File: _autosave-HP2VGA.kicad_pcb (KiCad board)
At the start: 4 copper layers, 40.6 x 63 mm, 141 parts, among them CON101 AVR-ISP-6, IC401 ATTINY87-AX, P101 CONN_02X10, P102 CONN_01X07, P103 CONN_02X08, P104 CONN_01X12, P105 CONN_01X02, P106 CONN_01X01, P107 CONN_01X01, P108 CONN_01X01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

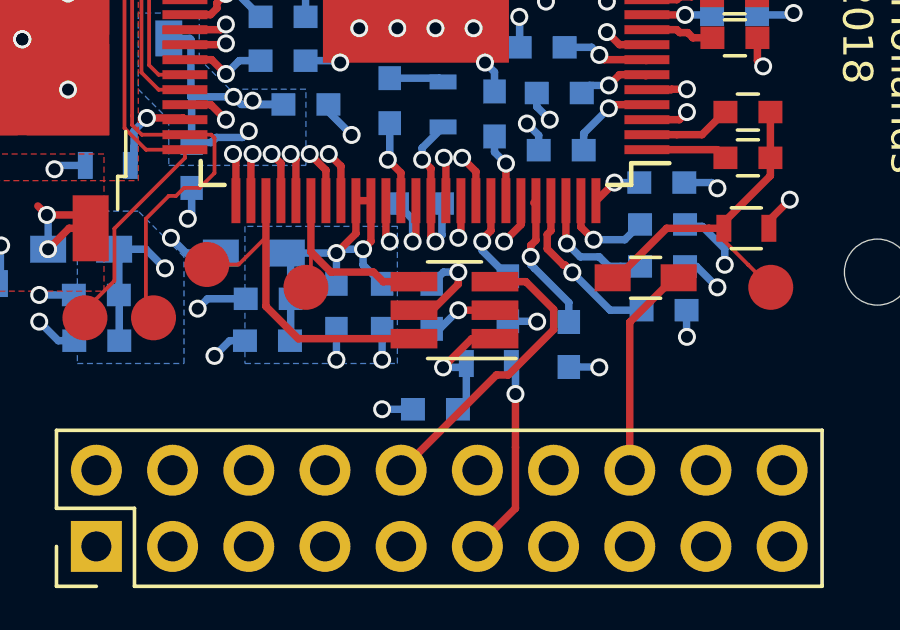
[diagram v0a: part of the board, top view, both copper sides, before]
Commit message: TX and RX accessing RAM. Sync not working.
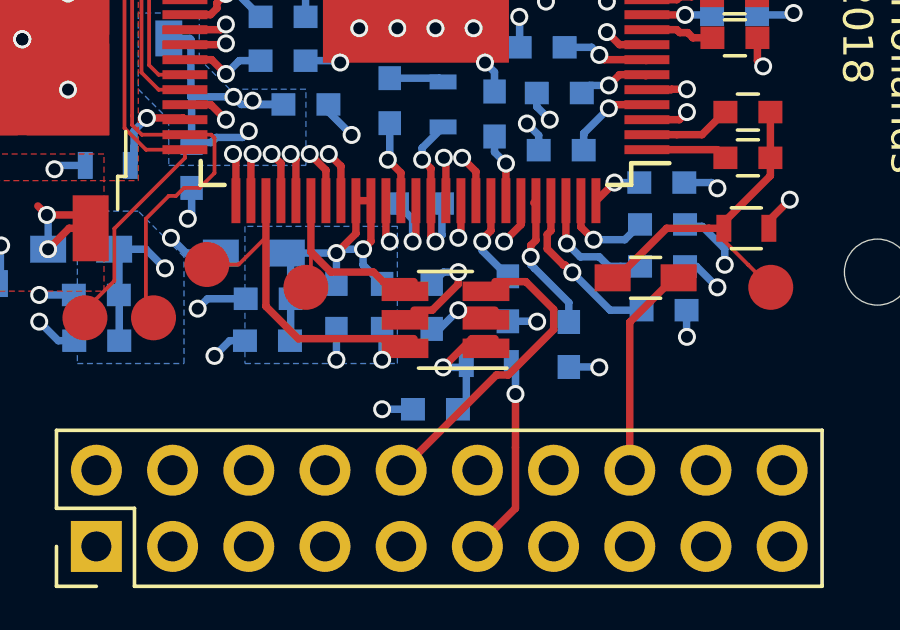
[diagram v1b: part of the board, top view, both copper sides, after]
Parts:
- moved U201 0.44 mm to (149.4, 78.8)
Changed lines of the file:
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@@
   )
   (module TO_SOT_Packages_SMD:SOT-23-6_Handsoldering (layer F.Cu)
-    (at 149.733 78.486 180)
+    (at 149.432 78.806 180)
     (descr "6-pin SOT-23 package, Handsoldering")
     (tags "SOT-23-6 Handsoldering")
